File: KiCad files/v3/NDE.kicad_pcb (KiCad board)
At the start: 2 copper layers, 90 x 90 mm, 27 parts, among them J1 Nabíjací modul, J10 Conn_01x01_Socket, J11 Conn_01x01_Socket, J12 Conn_01x01_Socket, J13 Conn_01x01_Socket, J14 VM_Select, J2 Step-up input, J3 Step-up output, J6 Conn_01x05_Socket, J7 Conn_01x08_Socket, J8 Conn_01x20_Socket, J9 Conn_01x20_Socket, U1 LM7805_TO220

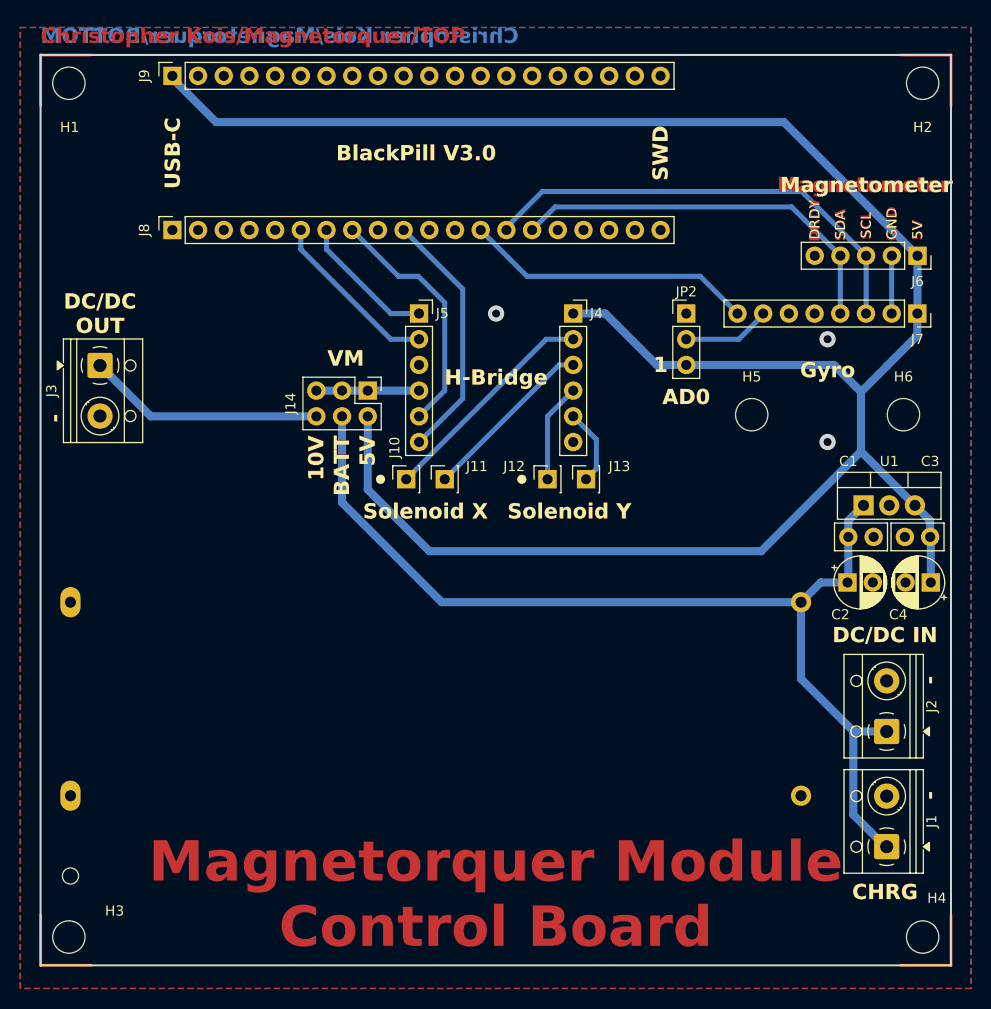
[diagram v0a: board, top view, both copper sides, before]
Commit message: Modified module pin spacing, thickened traces
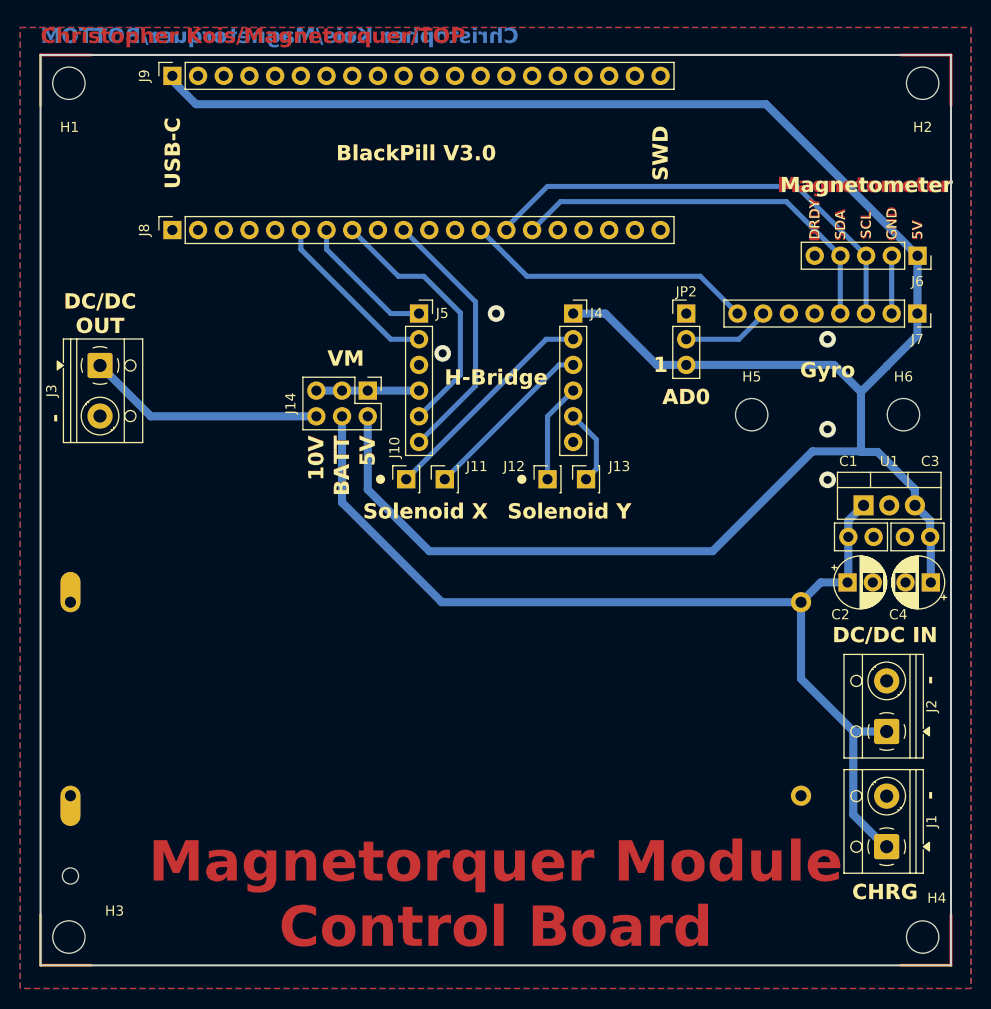
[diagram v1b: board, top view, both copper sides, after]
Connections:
- BT1 pad N1: Net-(BT1-PadN1) -> unconnected-(BT1-PadN1)
- BT1 pad P2: Net-(BT1-PadN1) -> unconnected-(BT1-PadP2)
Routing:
- net /BlackPill V3.0/A11: track 24.4 -> 26.0 mm
- net +5V: track 212.9 -> 214.0 mm
- net /BlackPill V3.0/A15: track 25.2 -> 26.2 mm
- net GND: vias 3 -> 5
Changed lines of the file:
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@@
 	)
 	(net 0 "")
-	(net 1 "Net-(BT1-PadN1)")
+	(net 1 "unconnected-(BT1-PadN1)")
 	(net 2 "GND")
 	(net 3 "+BATT")
@@
 	(net 52 "/BlackPill V3.0/B3")
 	(net 53 "/BlackPill V3.0/B10")
+	(net 54 "unconnected-(BT1-PadP2)")
 	(footprint "Capacitor_THT:CP_Radial_D5.0mm_P2.50mm"
 		(layer "F.Cu")
@@
 	)
 	(footprint "MountingHole:MountingHole_3.2mm_M3_ISO14580"
+		(locked yes)
 		(layer "F.Cu")
 		(at 170.3 85.565)
@@
 	)
 	(footprint "MountingHole:MountingHole_3.2mm_M3_ISO14580"
+		(locked yes)
 		(layer "F.Cu")
 		(at 185.3 85.565)
@@
 		(pad "N1" thru_hole oval
 			(at 36.11 9.565 180)
-			(size 2 3)
-			(drill 1.1)
+			(size 2 4)
+			(drill 1.1
+				(offset 0 1)
+			)
 			(layers "*.Cu" "*.Mask")
 			(remove_unused_layers no)
-			(net 1 "Net-(BT1-PadN1)")
-			(pintype "passive")
+			(net 1 "unconnected-(BT1-PadN1)")
+			(pintype "passive+no_connect")
 		)
 		(pad "N2" thru_hole oval
@@
 		(pad "P2" thru_hole oval
 			(at 36.11 -9.565 180)
-			(size 2 3)
-			(drill 1.1)
+			(size 2 4)
+			(drill 1.1
+				(offset 0 -1)
+			)
 			(layers "*.Cu" "*.Mask")
 			(remove_unused_layers no)
-			(net 1 "Net-(BT1-PadN1)")
-			(pintype "passive")
+			(net 54 "unconnected-(BT1-PadP2)")
+			(pintype "passive+no_connect")
 		)
 		(embedded_fonts no)
@@
 			(type default)
 		)
+		(locked yes)
 		(layer "Dwgs.User")
 	)
@@
 			(type default)
 		)
+		(locked yes)
 		(layer "Dwgs.User")
 	)
@@
 			(type default)
 		)
+		(locked yes)
 		(layer "Dwgs.User")
 	)
@@
 			(type default)
 		)
+		(locked yes)
 		(layer "Dwgs.User")
 	)
@@
 		)
 	)
-	(segment
-		(start 102.955 123.23)
-		(end 102.87 123.145)
-		(width 0.8)
-		(layer "F.Cu")
-		(net 1)
-	)
-	(segment
-		(start 102.87 104.185)
-		(end 102.955 104.1)
-		(width 0.8)
-		(layer "F.Cu")
-		(net 1)
-	)
 	(via
 		(at 145.034 75.565)
-		(size 1.6)
+		(size 1.65)
 		(drill 0.8)
 		(layers "F.Cu" "B.Cu")
@@
 	)
 	(via
-		(at 177.8 88.265)
-		(size 1.6)
+		(at 177.8 87)
+		(size 1.65)
 		(drill 0.8)
 		(layers "F.Cu" "B.Cu")
@@
 	(via
 		(at 177.8 78.105)
-		(size 1.6)
+		(size 1.65)
+		(drill 0.8)
+		(layers "F.Cu" "B.Cu")
+		(free yes)
+		(net 2)
+	)
+	(via
+		(at 139.75 79.5)
+		(size 1.65)
+		(drill 0.8)
+		(layers "F.Cu" "B.Cu")
+		(free yes)
+		(net 2)
+	)
+	(via
+		(at 177.8 92)
+		(size 1.65)
 		(drill 0.8)
 		(layers "F.Cu" "B.Cu")
@@
 	)
 	(segment
-		(start 132.34259 85.724999)
-		(end 132.34259 92.97259)
+		(start 186.436 92.936)
+		(end 182.75 89.25)
+		(width 0.8)
+		(layer "B.Cu")
+		(net 4)
+	)
+	(segment
+		(start 138.43 99.06)
+		(end 166.44 99.06)
 		(width 0.8)
 		(layer "B.Cu")
@@
 	)
 	(segment
+		(start 186.436 94.528)
+		(end 186.436 92.936)
+		(width 0.8)
+		(layer "B.Cu")
+		(net 4)
+	)
+	(segment
 		(start 178.435 80.645)
 		(end 181.107197 83.317197)
@@
 	)
 	(segment
+		(start 182.75 89.25)
+		(end 181.158 89.25)
+		(width 0.8)
+		(layer "B.Cu")
+		(net 4)
+	)
+	(segment
 		(start 187.94 96.032)
 		(end 186.436 94.528)
@@
 	)
 	(segment
-		(start 117.348 56.642)
-		(end 113.03 52.324)
+		(start 186.69 69.85)
+		(end 171.710518 54.870518)
+		(width 0.8)
+		(layer "B.Cu")
+		(net 4)
+	)
+	(segment
+		(start 132.34259 85.724999)
+		(end 132.34259 92.97259)
 		(width 0.8)
 		(layer "B.Cu")
@@
 	)
 	(segment
-		(start 113.03 52.324)
+		(start 113.03 52.53)
 		(end 113.03 52.07)
 		(width 0.8)
@@
 	)
 	(segment
-		(start 183.652394 80.761606)
-		(end 186.675 77.739)
+		(start 181.158 89.25)
+		(end 181.102 89.194)
 		(width 0.8)
 		(layer "B.Cu")
@@
 	)
 	(segment
-		(start 173.482 56.642)
-		(end 117.348 56.642)
+		(start 115.370518 54.870518)
+		(end 113.03 52.53)
 		(width 0.8)
 		(layer "B.Cu")
@@
 	)
 	(segment
-		(start 152.654 75.565)
-		(end 155.829 75.565)
+		(start 183.652394 80.761606)
+		(end 186.675 77.739)
 		(width 0.8)
 		(layer "B.Cu")
@@
 	)
 	(segment
-		(start 186.436 94.528)
-		(end 181.102 89.194)
+		(start 152.654 75.565)
+		(end 155.829 75.565)
 		(width 0.8)
 		(layer "B.Cu")
@@
 	)
 	(segment
-		(start 138.43 99.06)
-		(end 171.236 99.06)
+		(start 171.710518 54.870518)
+		(end 115.370518 54.870518)
 		(width 0.8)
 		(layer "B.Cu")
@@
 	)
 	(segment
-		(start 132.34259 92.97259)
-		(end 138.43 99.06)
+		(start 176.306 89.194)
+		(end 181.102 89.194)
 		(width 0.8)
 		(layer "B.Cu")
@@
 	)
 	(segment
-		(start 186.69 69.85)
-		(end 173.482 56.642)
+		(start 166.44 99.06)
+		(end 176.306 89.194)
 		(width 0.8)
 		(layer "B.Cu")
@@
 	)
 	(segment
-		(start 171.236 99.06)
-		(end 181.102 89.194)
+		(start 132.34259 92.97259)
+		(end 138.43 99.06)
 		(width 0.8)
 		(layer "B.Cu")
@@
 	)
 	(segment
-		(start 135.382 71.882)
-		(end 130.81 67.31)
+		(start 137.414 85.725)
+		(end 141.5 81.639)
 		(width 0.5)
 		(layer "B.Cu")
@@
 	)
 	(segment
-		(start 137.350304 71.882)
-		(end 135.382 71.882)
+		(start 135.382 71.882)
+		(end 130.81 67.31)
 		(width 0.5)
 		(layer "B.Cu")
@@
 	)
 	(segment
-		(start 137.414 85.725)
-		(end 139.954 83.184999)
+		(start 141.5 81.639)
+		(end 141.5 75.5)
 		(width 0.5)
 		(layer "B.Cu")
@@
 	)
 	(segment
-		(start 139.954 74.485696)
-		(end 137.350304 71.882)
+		(start 141.5 75.5)
+		(end 137.882 71.882)
 		(width 0.5)
 		(layer "B.Cu")
@@
 	)
 	(segment
-		(start 139.954 83.184999)
-		(end 139.954 74.485696)
+		(start 137.882 71.882)
+		(end 135.382 71.882)
 		(width 0.5)
 		(layer "B.Cu")
@@
 	)
 	(segment
-		(start 141.732 83.980469)
-		(end 141.732 73.152)
+		(start 143 74.42)
+		(end 135.89 67.31)
 		(width 0.5)
 		(layer "B.Cu")
@@
 	)
 	(segment
-		(start 141.732 73.152)
-		(end 135.89 67.31)
+		(start 143 82.712469)
+		(end 143 74.42)
 		(width 0.5)
 		(layer "B.Cu")
@@
 	(segment
 		(start 137.447469 88.265)
-		(end 141.732 83.980469)
+		(end 143 82.712469)
 		(width 0.5)
 		(layer "B.Cu")
@@
 	)
 	(segment
-		(start 149.606 63.5)
-		(end 175.26 63.5)
+		(start 150.106 63)
+		(end 174.76 63)
 		(width 0.5)
 		(layer "B.Cu")
@@
 	)
 	(segment
-		(start 146.05 67.056)
-		(end 149.606 63.5)
+		(start 181.61 75.55)
+		(end 181.595 75.565)
 		(width 0.5)
 		(layer "B.Cu")
@@
 	)
 	(segment
-		(start 175.26 63.5)
-		(end 181.61 69.85)
+		(start 146.05 67.31)
+		(end 146.05 67.056)
 		(width 0.5)
 		(layer "B.Cu")
@@
 	)
 	(segment
-		(start 146.05 67.31)
-		(end 146.05 67.056)
+		(start 146.05 67.056)
+		(end 150.106 63)
 		(width 0.5)
 		(layer "B.Cu")
@@
 	)
 	(segment
-		(start 181.61 75.55)
-		(end 181.595 75.565)
+		(start 181.61 69.85)
+		(end 181.61 75.55)
 		(width 0.5)
 		(layer "B.Cu")
@@
 	)
 	(segment
-		(start 181.61 69.85)
-		(end 181.61 75.55)
+		(start 174.76 63)
+		(end 181.61 69.85)
 		(width 0.5)
 		(layer "B.Cu")
@@
 	)
 	(segment
-		(start 174.244 65.024)
-		(end 150.876 65.024)
+		(start 179.07 69.85)
+		(end 173.72 64.5)
 		(width 0.5)
 		(layer "B.Cu")
@@
 	)
 	(segment
-		(start 179.07 69.85)
-		(end 174.244 65.024)
+		(start 151.4 64.5)
+		(end 148.59 67.31)
 		(width 0.5)
 		(layer "B.Cu")
@@
 	)
 	(segment
-		(start 179.055 69.865)
-		(end 179.07 69.85)
+		(start 173.72 64.5)
+		(end 151.4 64.5)
 		(width 0.5)
 		(layer "B.Cu")
@@
 	)
 	(segment
-		(start 150.876 65.024)
-		(end 148.59 67.31)
+		(start 179.055 69.865)
+		(end 179.07 69.85)
 		(width 0.5)
 		(layer "B.Cu")
@@
 	)
 	(group ""
+		(locked yes)
 		(members "9ec4260f-7db1-47cc-9553-d887738c5a1d" "a83c846c-c5c2-4ea1-bd42-579bea81c444"
 			"bae8a071-f9cb-464d-92ee-856b7329690e"
@@
 	)
 	(group ""
+		(locked yes)
 		(members "25f1e8ed-6469-450a-ad16-d1ad0f36db13" "463ddaa0-f55e-4058-92ee-94b53879c1e5"
 			"8dba86ce-8e8c-4b76-9152-6bc9a735385d"
